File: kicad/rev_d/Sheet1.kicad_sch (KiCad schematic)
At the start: 159 parts, among them J1 JUMPER, J2 JUMPER, J3 JUMPER, J4 JUMPER, J7 JUMPER, Q1 QUARTZ, X1 FDD34M, X2 IDE40M, X3 IDC26LPT, X7 DB15VGA, X8 PLB1-4I, X9 PLB1-2

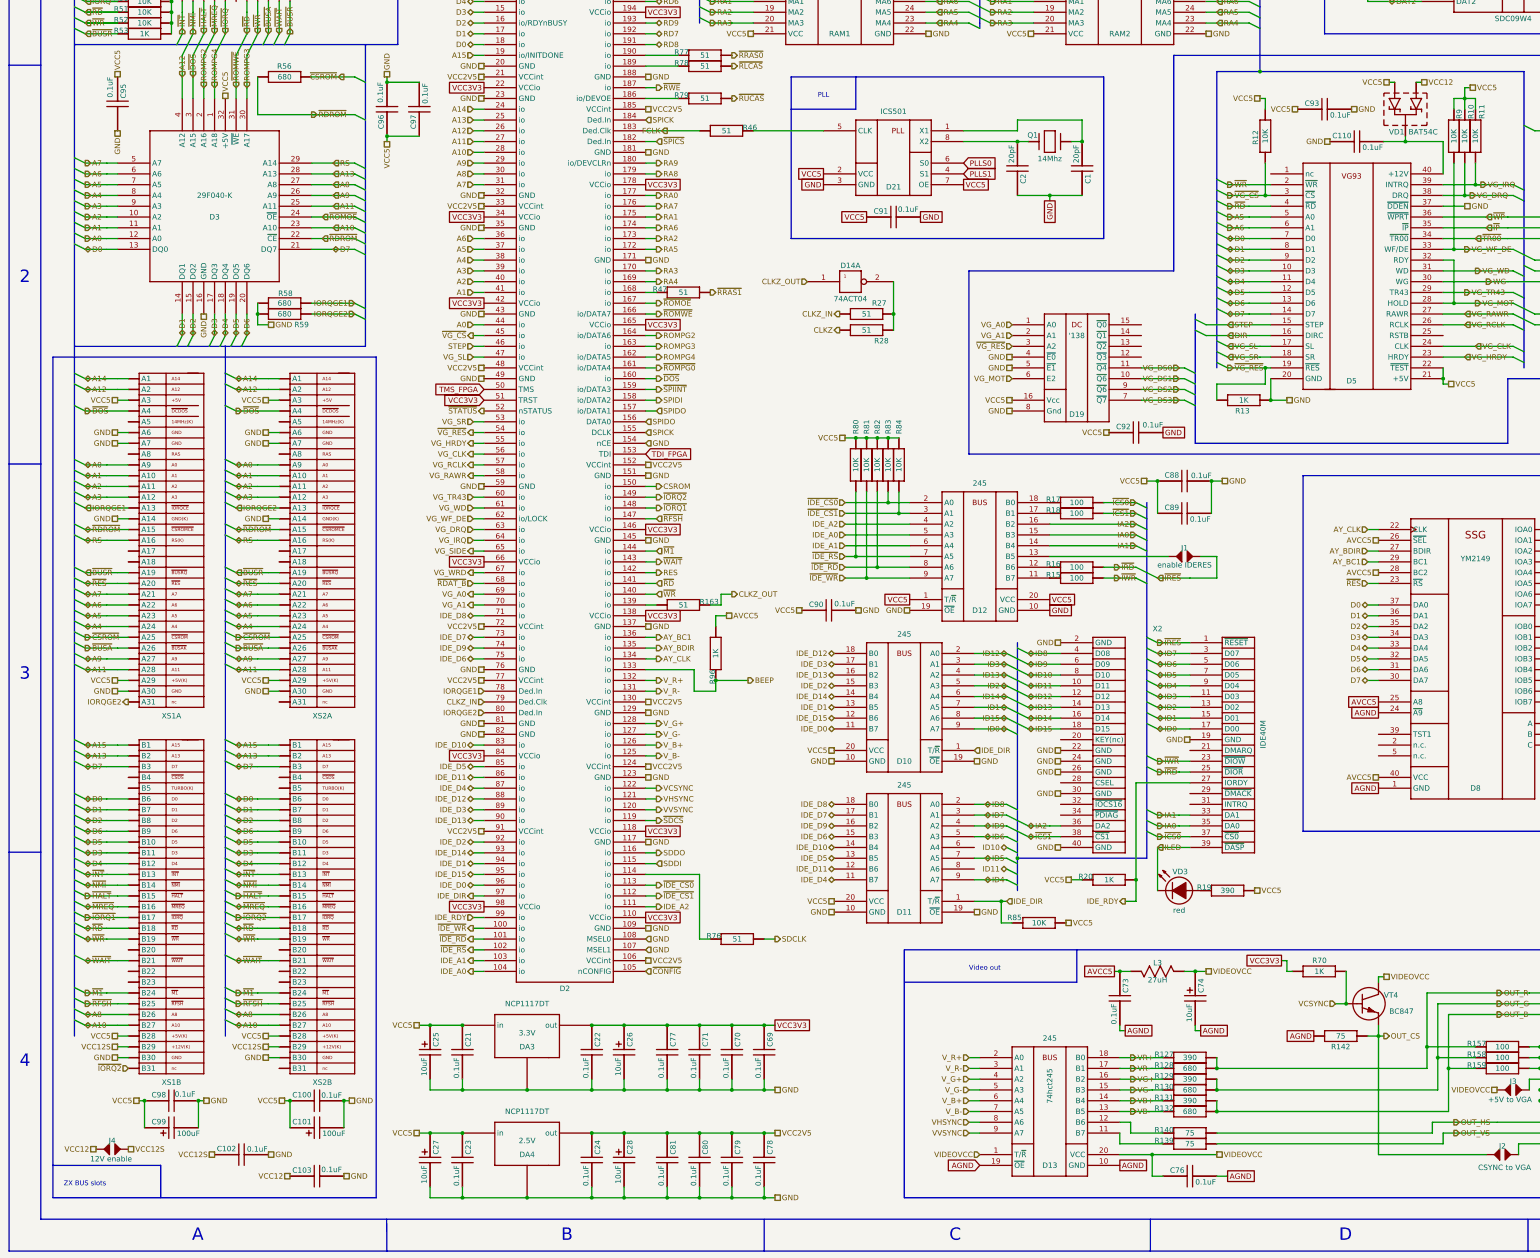
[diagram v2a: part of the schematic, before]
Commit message: pentevo: small update to converted kicad sch (serial, power, tape)
git-svn-id: svn://localhost/local-pentevo@1176 c6c76956-fad2-4150-a3a9-ea0a427205ba
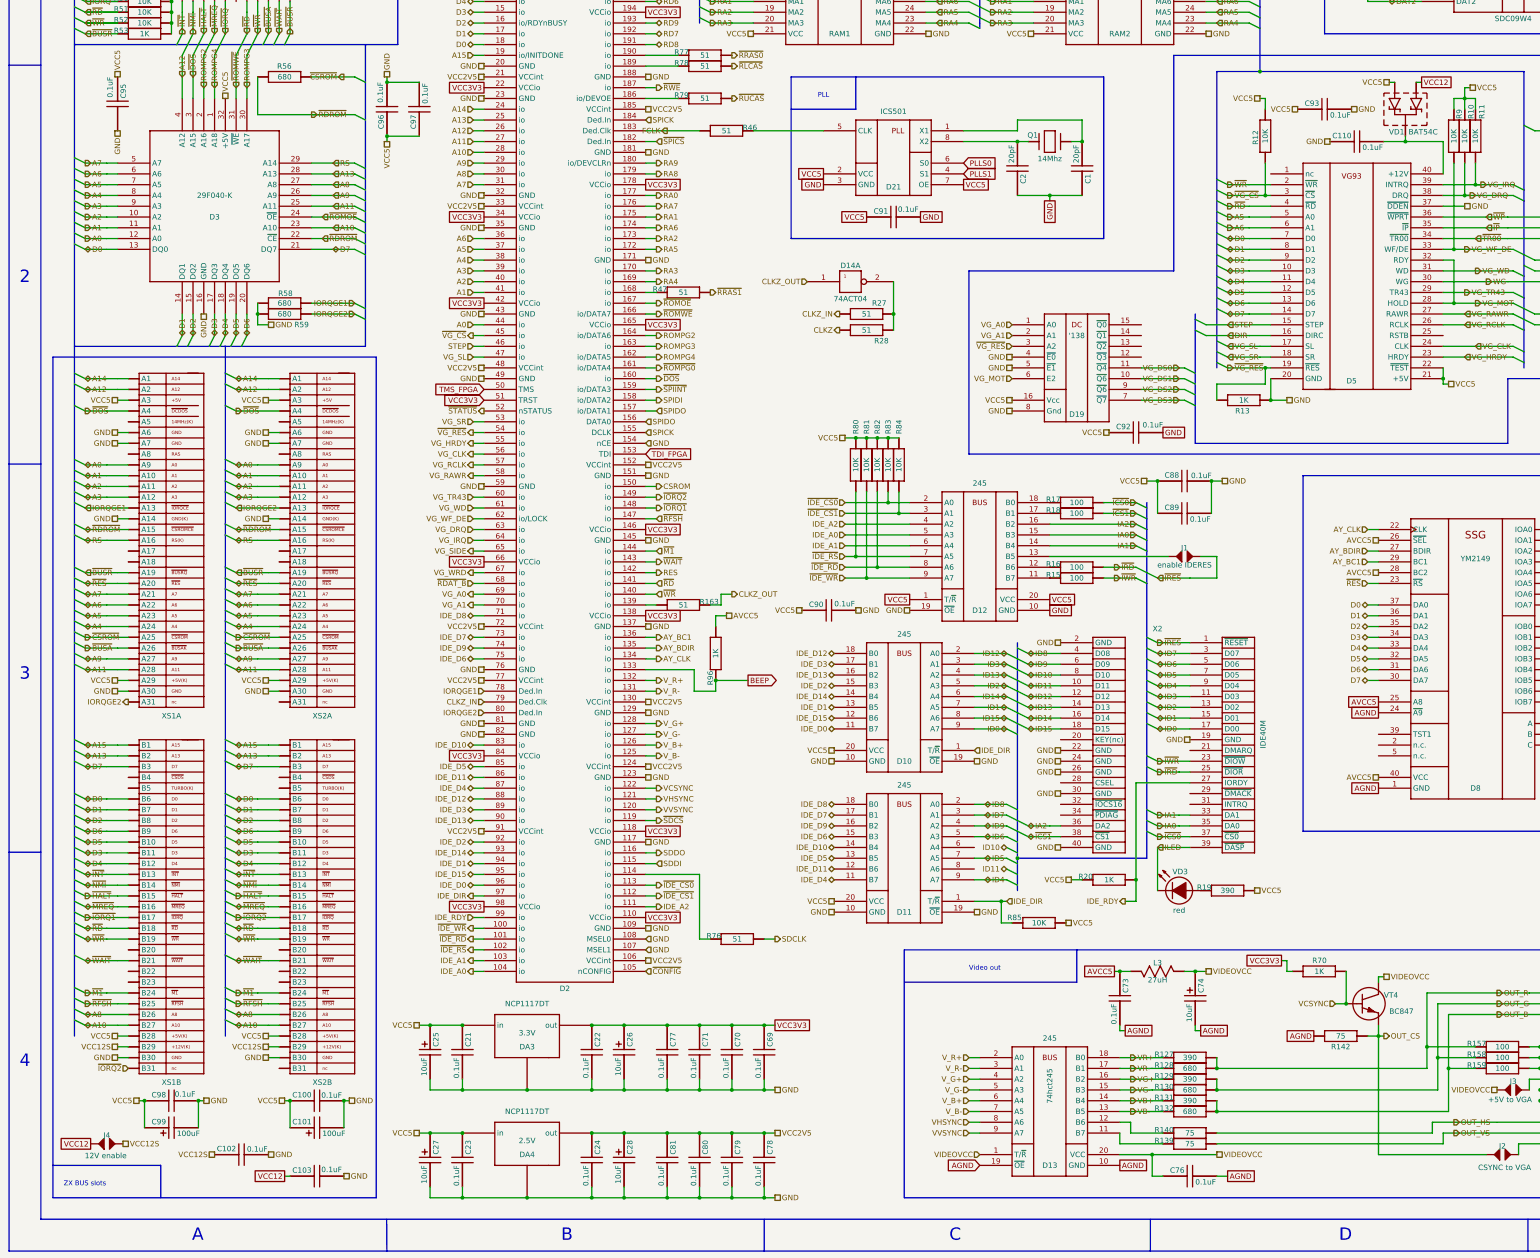
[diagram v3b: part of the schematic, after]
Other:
- moved on the sheet: J4
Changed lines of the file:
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@@
 	(wire
 		(pts
+			(xy 74.93 401.32) (xy 76.2 401.32)
+		)
+		(stroke
+			(width 0)
+			(type default)
+		)
+	)
+	(wire
+		(pts
 			(xy 27.94 172.72) (xy 33.02 172.72)
 		)
@@
 		)
 	)
+	(global_label "VCC12"
+		(shape passive)
+		(at 74.93 401.32 180)
+		(fields_autoplaced yes)
+		(effects
+			(font
+				(size 1.27 1.27)
+			)
+			(justify right)
+		)
+		(property "Intersheetrefs" "${INTERSHEET_REFS}"
+			(at 67.0085 401.32 0)
+			(effects
+				(font
+					(size 1.27 1.27)
+				)
+				(justify right)
+				(hide yes)
+			)
+		)
+	)
 	(global_label "VCC3V3"
 		(shape passive)
@@
 		)
 	)
+	(global_label "BEEP"
+		(shape output)
+		(at 184.15 284.48 0)
+		(fields_autoplaced yes)
+		(effects
+			(font
+				(size 1.27 1.27)
+			)
+			(justify left)
+		)
+		(property "Intersheetrefs" "${INTERSHEET_REFS}"
+			(at 191.9732 284.48 0)
+			(effects
+				(font
+					(size 1.27 1.27)
+				)
+				(justify left)
+				(hide yes)
+			)
+		)
+	)
 	(global_label "VCC3V3"
 		(shape passive)
@@
 		)
 	)
+	(global_label "VCC12"
+		(shape passive)
+		(at 342.9 143.51 0)
+		(fields_autoplaced yes)
+		(effects
+			(font
+				(size 1.27 1.27)
+			)
+			(justify left)
+		)
+		(property "Intersheetrefs" "${INTERSHEET_REFS}"
+			(at 350.8215 143.51 0)
+			(effects
+				(font
+					(size 1.27 1.27)
+				)
+				(justify left)
+				(hide yes)
+			)
+		)
+	)
 	(global_label "VCC3V3"
 		(shape passive)
@@
 		)
 	)
+	(global_label "VCC12"
+		(shape passive)
+		(at 29.21 393.7 180)
+		(fields_autoplaced yes)
+		(effects
+			(font
+				(size 1.27 1.27)
+			)
+			(justify right)
+		)
+		(property "Intersheetrefs" "${INTERSHEET_REFS}"
+			(at 21.2885 393.7 0)
+			(effects
+				(font
+					(size 1.27 1.27)
+				)
+				(justify right)
+				(hide yes)
+			)
+		)
+	)
 	(global_label "VCC3V3"
 		(shape passive)
@@
 		)
 	)
-	(hierarchical_label "VCC12"
-		(shape passive)
-		(at 30.48 394.97 180)
-		(fields_autoplaced yes)
-		(effects
-			(font
-				(size 1.27 1.27)
-			)
-			(justify right)
-		)
-	)
 	(hierarchical_label "A2"
 		(shape input)
@@
 		)
 	)
-	(hierarchical_label "BEEP"
-		(shape output)
-		(at 184.15 284.48 0)
-		(fields_autoplaced yes)
-		(effects
-			(font
-				(size 1.27 1.27)
-			)
-			(justify left)
-		)
-	)
 	(hierarchical_label "~{RUCAS}"
 		(shape input)
@@
 	(hierarchical_label "VCC12S"
 		(shape passive)
-		(at 38.1 394.97 0)
+		(at 36.83 393.7 0)
 		(fields_autoplaced yes)
 		(effects
@@
 		)
 	)
-	(hierarchical_label "VCC12"
-		(shape passive)
-		(at 76.2 401.32 180)
-		(fields_autoplaced yes)
-		(effects
-			(font
-				(size 1.27 1.27)
-			)
-			(justify right)
-		)
-	)
 	(hierarchical_label "VG_RAWR"
 		(shape input)
@@
 		)
 	)
-	(hierarchical_label "VCC12"
-		(shape passive)
-		(at 342.9 143.51 0)
-		(fields_autoplaced yes)
-		(effects
-			(font
-				(size 1.27 1.27)
-			)
-			(justify left)
-		)
-	)
 	(hierarchical_label "DAT2"
 		(shape bidirectional)
@@
 		(dnp no)
 		(property "Reference" "R96"
-			(at 176.53 281.94 90)
+			(at 176.022 282.194 90)
 			(effects
 				(font
@@
 	(symbol
 		(lib_id "eva-altium-import:Sheet1_0_JUMPER")
-		(at 30.48 394.97 0)
+		(at 29.21 393.7 0)
 		(unit 1)
 		(exclude_from_sim no)
@@
 		(dnp no)
 		(property "Reference" "J4"
-			(at 34.29 393.7 0)
+			(at 33.02 392.43 0)
 			(effects
 				(font
@@
 		)
 		(property "Value" "JUMPER"
-			(at 30.48 394.97 0)
+			(at 29.21 393.7 0)
 			(effects
 				(font
@@
 		)
 		(property "Footprint" "JUMPER"
-			(at 30.48 394.97 0)
+			(at 29.21 393.7 0)
 			(effects
 				(font
@@
 		)
 		(property "Datasheet" ""
-			(at 30.48 394.97 0)
+			(at 29.21 393.7 0)
 			(effects
 				(font
@@
 		)
 		(property "Description" "12V enable"
-			(at 34.036 397.256 0)
+			(at 32.766 396.494 0)
 			(effects
 				(font
@@
 		)
 		(property "ALTIUM_VALUE" "*"
-			(at 30.48 394.97 0)
+			(at 29.21 393.7 0)
 			(effects
 				(font
@@
 		)
 		(property "DESCRIPTION" "enable IDERES"
-			(at 34.29 396.24 0)
+			(at 33.02 394.97 0)
 			(effects
 				(font

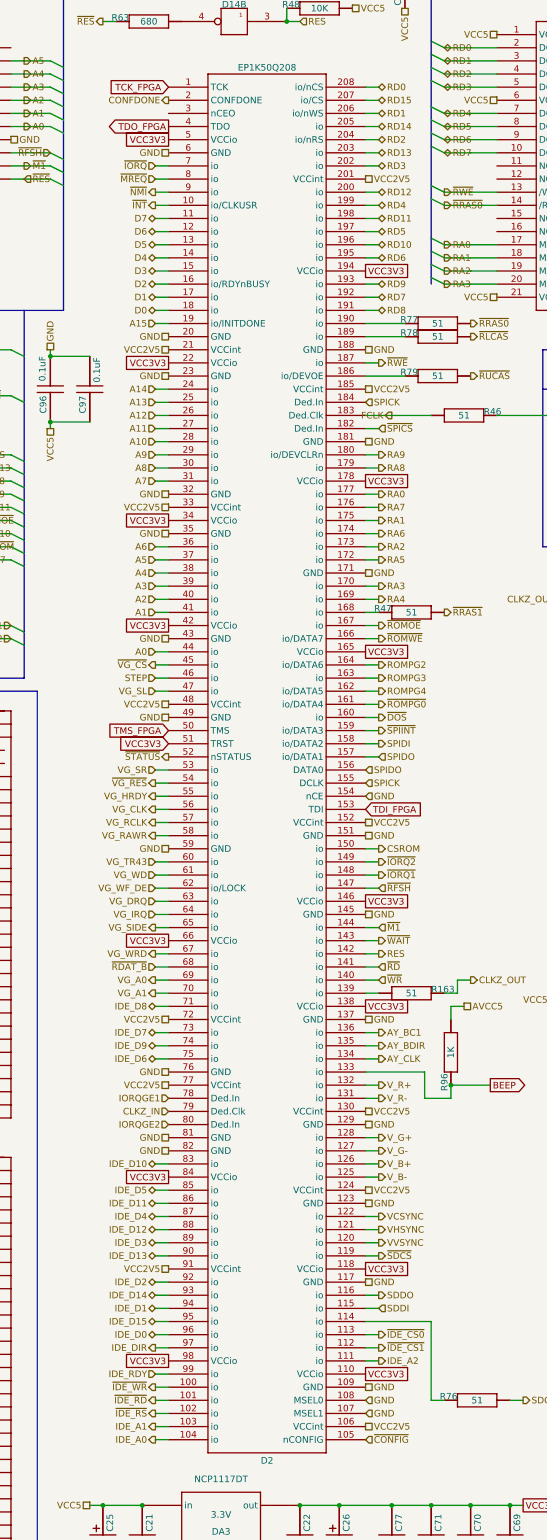
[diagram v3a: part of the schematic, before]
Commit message: pentevo: small update to converted kicad sch (AVR)
git-svn-id: svn://localhost/local-pentevo@1178 c6c76956-fad2-4150-a3a9-ea0a427205ba
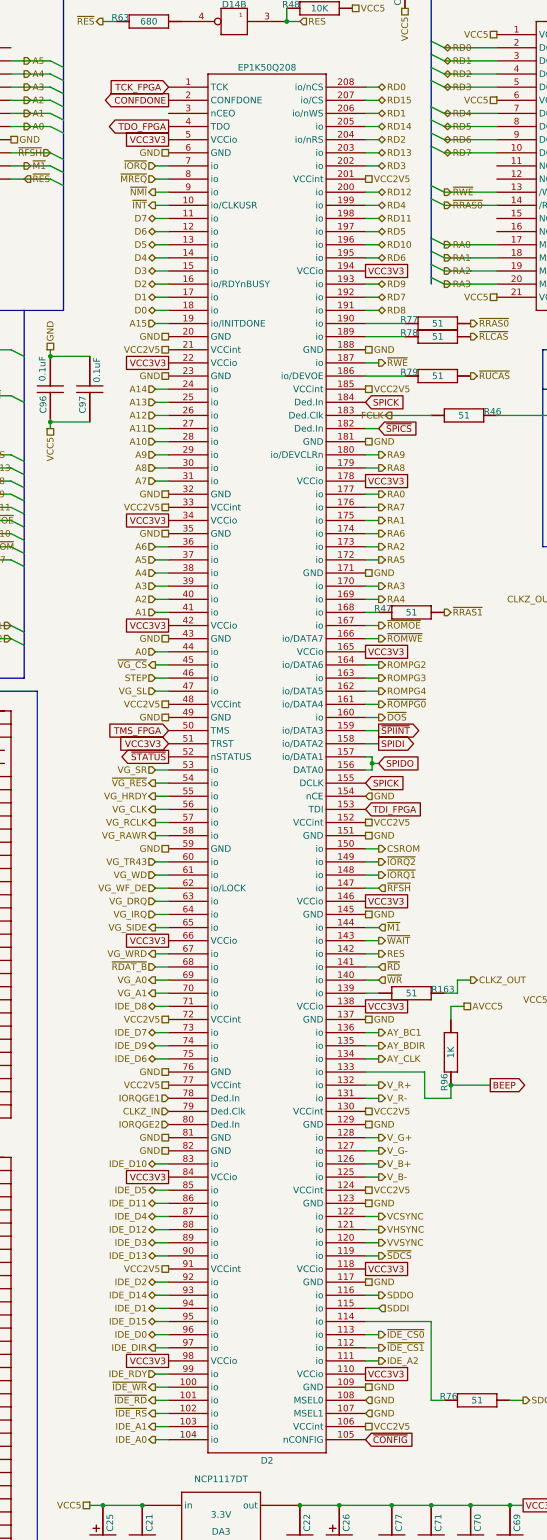
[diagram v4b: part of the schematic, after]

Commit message: fix scheme: - Remove netbuses; - Sets ports to global marks.
git-svn-id: svn://localhost/local-pentevo@1179 c6c76956-fad2-4150-a3a9-ea0a427205ba
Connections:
- net GND: no longer D18.5, X3.23 (PE)
- net ID10: now also D11.6 (A4)
- net ID11: now also D11.8 (A6)
- new net PR_PE: D18.5, X3.23 (PE)
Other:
- note added: "DRAM"
- moved on the sheet: C1, C106, C107, C108, C109, C2, C3, C50, C82, C86, C87, C91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

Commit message: pentevo: fix ALTIUM_VALUE to Value, add microSD card
git-svn-id: svn://localhost/local-pentevo@1187 c6c76956-fad2-4150-a3a9-ea0a427205ba
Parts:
- C1, C2: value CAPCHIP -> 20pF; ALTIUM_VALUE 20pF -> (none)
- C100, C102, C103, C104, C106, C107, C108, C109, C110, C21, C22, C23, C24, C50, C69, C70, C71, C73, C76, C77, C78, C79, C80, C81, C82, C86, C87, C88, C89, C90, C91, C92, C93, C94, C95, C96, C97, C98: value CAPCHIP -> 0.1uF; ALTIUM_VALUE 0.1uF -> (none)
- C101, C99: value ECAPCHIPB -> 100uF; ALTIUM_VALUE 100uF -> (none)
- C25, C26, C27, C28, C3, C74: value ECAPCHIP -> 10uF; ALTIUM_VALUE 10uF -> (none)
- D6: value '06 -> *; ALTIUM_VALUE * -> (none)
- DA3: value NCP1117DT -> 3.3V; ALTIUM_VALUE 3.3V -> (none)
- DA4: value NCP1117DT -> 2.5V; ALTIUM_VALUE 2.5V -> (none)
- L1: value L-CHIP -> 1uH; ALTIUM_VALUE 1uH -> (none)
- L3: value CDR64B -> 27uH; ALTIUM_VALUE 27uH -> (none)
- Q1: value QUARTZ -> 14Mhz; ALTIUM_VALUE 14Mhz -> (none)
- R1, R10, R11, R12, R14, R2, R21, R3, R4, R48, R49, R50, R51, R52, R80, R81, R82, R83, R84, R85, R9: value RESCHIP -> 10K; ALTIUM_VALUE 10K -> (none)
- R127, R129, R131, R19: value RESCHIP -> 390; ALTIUM_VALUE 390 -> (none)
- R128, R130, R132, R29, R56, R57, R58, R59, R63, R64, R65, R66, R67, R68: value RESCHIP -> 680; ALTIUM_VALUE 680 -> (none)
- R13, R20, R5, R53, R54, R55, R6, R69, R7, R70, R8, R96: value RESCHIP -> 1K; ALTIUM_VALUE 1K -> (none)
- R139, R140, R142: value RESCHIP -> 75; ALTIUM_VALUE 75 -> (none)
- R15, R157, R158, R159, R16, R17, R18: value RESCHIP -> 100; ALTIUM_VALUE 100 -> (none)
- R163, R27, R28, R46, R47, R76, R77, R78, R79: value RESCHIP -> 51; ALTIUM_VALUE 51 -> (none)

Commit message: pentevo: add 9pin aafp/ac97 audio, change usb conn to type C, add extra SS14 in addition to BAT54C for mega power, replace '245s footprints with TSSOP, add resistors to MREQ/IORQ/RD/WR
git-svn-id: svn://localhost/local-pentevo@1188 c6c76956-fad2-4150-a3a9-ea0a427205ba
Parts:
- added R146, R147, R148, R149: 51, R-CHIP, symbol eva-altium-import:Sheet1_0_RESCHIP
- D10, D11, D12, D13, D17: footprint SOL20 -> Package_SO:TSSOP-20_4.4x6.5mm_P0.65mm
- D6: value * -> '06
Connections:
- net ~{IORQ}: now also R148.1 (i/o); no longer D1.16 (~{IORQ})
- net ~{MREQ}: now also R149.1 (i/o); no longer D1.15 (~{MREQ})
- net ~{RD}: now also R147.1 (i/o); no longer D1.18 (~{RD})
- net ~{WR}: now also R146.1 (i/o); no longer D1.19 (~{WR})
- new net: D1.16 (~{IORQ}), R148.2 (i/o1)
- new net: D1.18 (~{RD}), R147.2 (i/o1)
- new net: D1.15 (~{MREQ}), R149.2 (i/o1)
- new net: D1.19 (~{WR}), R146.2 (i/o1)
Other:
- moved on the sheet: D1, R49, R50, R51, R52, R53, R64, R66, R67

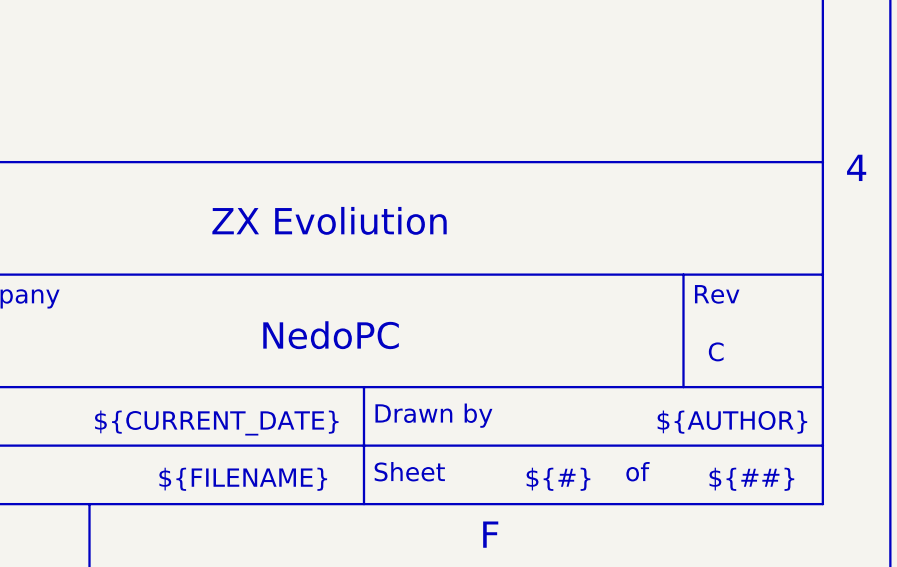
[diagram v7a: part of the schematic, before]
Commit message: pentevo: fix evolIution -> evolution
git-svn-id: svn://localhost/local-pentevo@1189 c6c76956-fad2-4150-a3a9-ea0a427205ba
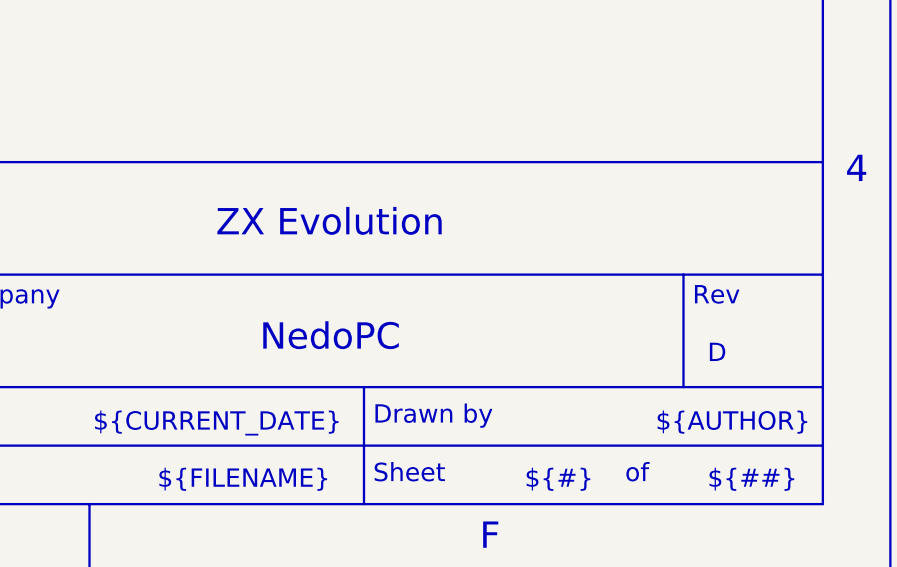
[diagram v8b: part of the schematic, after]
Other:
- title: ZX Evoliution -> ZX Evolution
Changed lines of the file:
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@@
 	(paper "User" 558.8 431.8)
 	(title_block
-		(title "ZX Evoliution")
-		(rev "C")
+		(title "ZX Evolution")
+		(rev "D")
 		(company "NedoPC")
 	)
